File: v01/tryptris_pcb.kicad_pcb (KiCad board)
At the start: 2 copper layers, 133 parts, among them J1 USB_C_Receptacle_USB2.0, J2 I2C-L, J3 I2C-R, SW1 Reset, U1 ATmega32U4-AU, U2 MCP23017_SO, Y1 16Mhz

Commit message: PCB components roughly placed
* Removed duplicate resistors on D- and D+
* Roughly placed all components. MCU and IO expander and resistors are
  all on the back to save board space. I'm hoping that the board can fit
  inside the existing switch place outline.
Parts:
- removed R6, R7: 22, Resistor_SMD:R_0805_2012Metric
- C1, C2, C3, C4, C5, C6, C7, F2, J1, J2, J3, R10, R2, R3, R4, R5, R8, R9, U1, U2, Y1: moved to B.Cu
- moved R1 337.2 mm to (52.6, 34.3), turned to 270 degrees
- moved C5 318.2 mm to (92.6, 111.6), turned to 90 degrees
- moved C3 308.0 mm to (101.2, 97.3), turned to 90 degrees
- moved C6 306.3 mm to (103.4, 97.3), turned to 90 degrees
- moved U1 298.2 mm to (100.9, 108.1), turned to 270 degrees
- moved C2 289.5 mm to (112.5, 103.6), turned to 180 degrees
- moved C4 285.8 mm to (92.6, 105.1), turned to 270 degrees
- moved Y1 285.0 mm to (112.5, 107.1), turned to 90 degrees
- moved C1 275.8 mm to (112.5, 110.5)
- moved R8 221.3 mm to (95.8, 116.2)
- moved C7 201.5 mm to (106.0, 116.2)
- moved D45 145.2 mm to (314.6, 79.6)
- moved MX28 142.5 mm to (224.3, 45.1)
- moved D39 129.8 mm to (314.6, 60.7)
- moved R10 124.7 mm to (207.0, 118.0), turned to 180 degrees
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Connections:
- U1 pad 3: Net-(R7-Pad1) -> D-
- U1 pad 4: Net-(R6-Pad1) -> D+

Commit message: Made progress on the left side routing.
I am going to put the components on the bottom (except diodes), and
ports on the top so that the board can be lower to the table.

A bunch of routing for the left side is done after a few different
attempts.
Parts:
- J1: moved to F.Cu
- R1: moved to B.Cu
- moved R3 40.9 mm to (71.2, 30.9), turned to 270 degrees
- moved F2 31.2 mm to (73.7, 36.6)
- moved C2 31.1 mm to (83.0, 113.5), turned to 0 degrees
- moved C1 29.7 mm to (83.0, 106.6), turned to 180 degrees
- moved Y1 29.6 mm to (83.0, 110.0), turned to 270 degrees
- moved R2 29.0 mm to (83.2, 34.4), turned to 180 degrees
- moved R4 27.2 mm to (77.1, 47.4)
- moved C6 25.2 mm to (92.2, 119.8), turned to 270 degrees
- moved J1 25.1 mm to (77.6, 26.1), turned to 180 degrees
- moved C3 23.6 mm to (94.3, 119.8), turned to 270 degrees
- moved C7 22.2 mm to (90.6, 100.3), turned to 180 degrees
- moved R5 21.4 mm to (80.8, 47.4)
- moved R8 16.4 mm to (99.6, 100.3), turned to 180 degrees
- moved C4 14.0 mm to (104.4, 112.6), turned to 0 degrees
- moved C5 13.6 mm to (104.6, 105.2), turned to 0 degrees
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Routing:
- net GND: track 0.00 -> 202.3 mm, vias 0 -> 2
- net Row0-L: track 0.00 -> 197.0 mm, vias 0 -> 1
- net Row1-L: track 0.00 -> 169.9 mm, vias 0 -> 1
- net +5V: track 0.00 -> 159.4 mm, vias 0 -> 6
- net Row2-L: track 0.00 -> 149.6 mm, vias 0 -> 1
- net Col0: track 0.00 -> 127.7 mm
- net Row3-L: track 0.00 -> 126.2 mm, vias 0 -> 1
- net Col1: track 0.00 -> 124.4 mm
- net Net-(R1-Pad2): track 0.00 -> 110.9 mm
- net Col4: track 0.00 -> 97.6 mm
- net Col2: track 0.00 -> 96.6 mm, vias 0 -> 1
- net D-: track 0.00 -> 88.0 mm, vias 0 -> 2
- net D+: track 0.00 -> 83.8 mm, vias 0 -> 2
- net Col5: track 0.00 -> 60.0 mm
- net Col3: track 0.00 -> 57.0 mm
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- added copper zone on F.Cu, net (none)
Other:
- board outline added: 298.2 x 124.6 mm
- net class power added: clearance 0.2, trace_width 0.375, via_dia 0.8, via_drill 0.4

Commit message: Fiddle with wiring more.
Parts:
- J2: moved to F.Cu
- moved J2 19.8 mm to (142.9, 108.9), turned to 0 degrees
- renumbered F2 to F1
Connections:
- D25 pad 1: Row4L -> Row4-L
- D26 pad 1: Row4L -> Row4-L
- D27 pad 1: Row4L -> Row4-L
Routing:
- net Row4-L: track 0.00 -> 80.4 mm, vias 0 -> 1
- net Col3: track 57.0 -> 124.4 mm, vias 0 -> 1
- net Row4L: track 55.3 -> 0.00 mm
- net Col5: track 60.0 -> 105.3 mm
- net Col4: track 97.6 -> 126.3 mm, vias 0 -> 2
- net Net-(J1-PadB5): track 6.08 -> 8.14 mm, vias 0 -> 1
- net SCL-L: track 1.56 -> 0.00 mm
- net VCC: track 14.1 -> 14.4 mm, vias 2 -> 0
- added copper zone on B.Cu, net GND
- added copper zone on F.Cu, net GND
- removed copper zone on F.Cu, net (none)

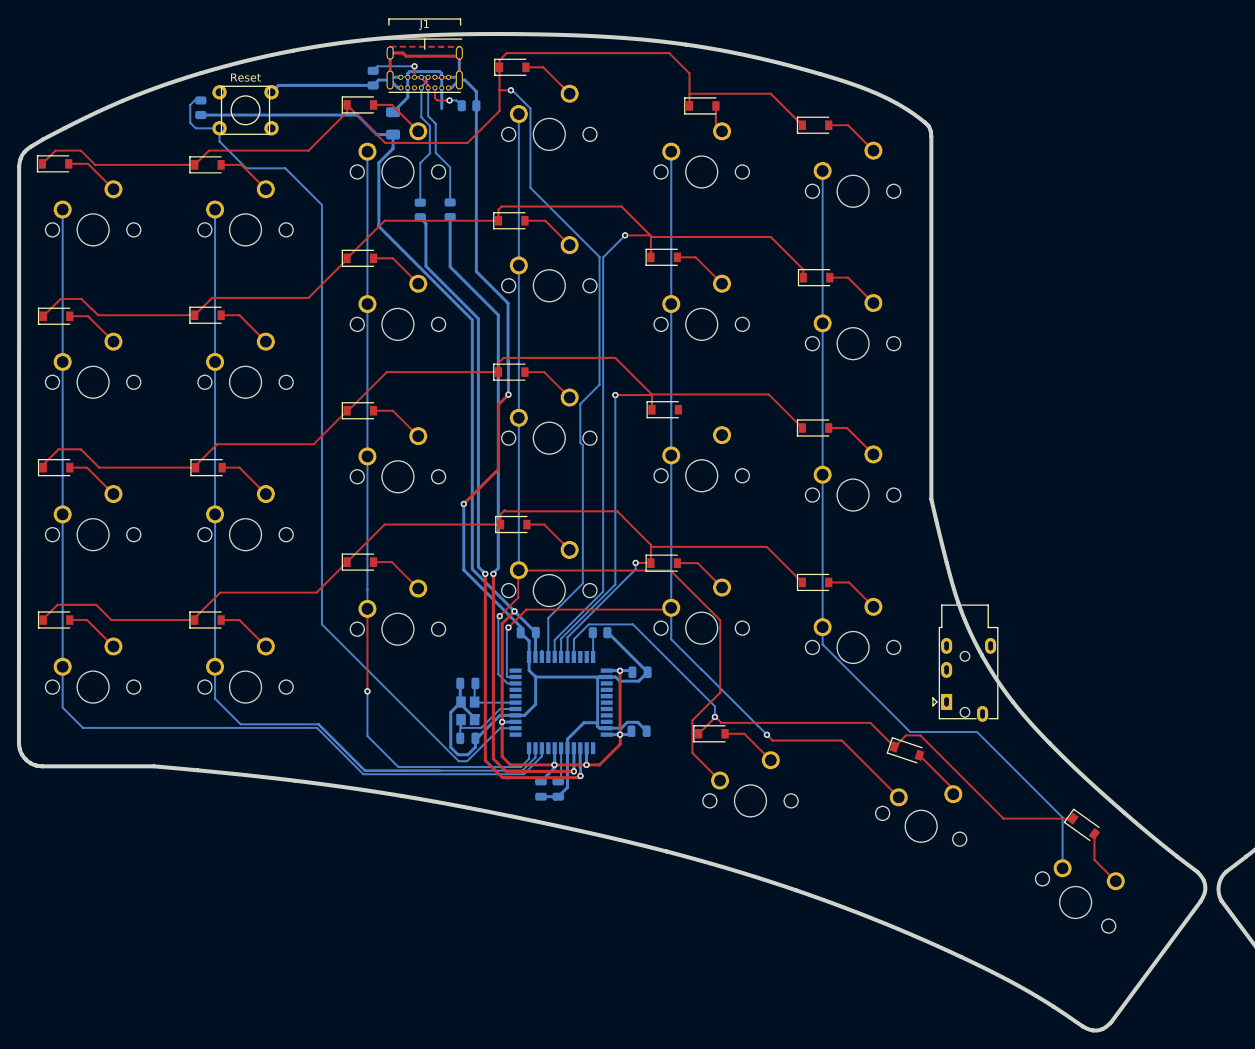
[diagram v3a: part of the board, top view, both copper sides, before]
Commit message: Move components to a block outside the switch matrix
* Having the ports top mounted will let the board be lower profile.
* Having the components on top looks kind of cool too.
* Roughly routed the entire left sideci!
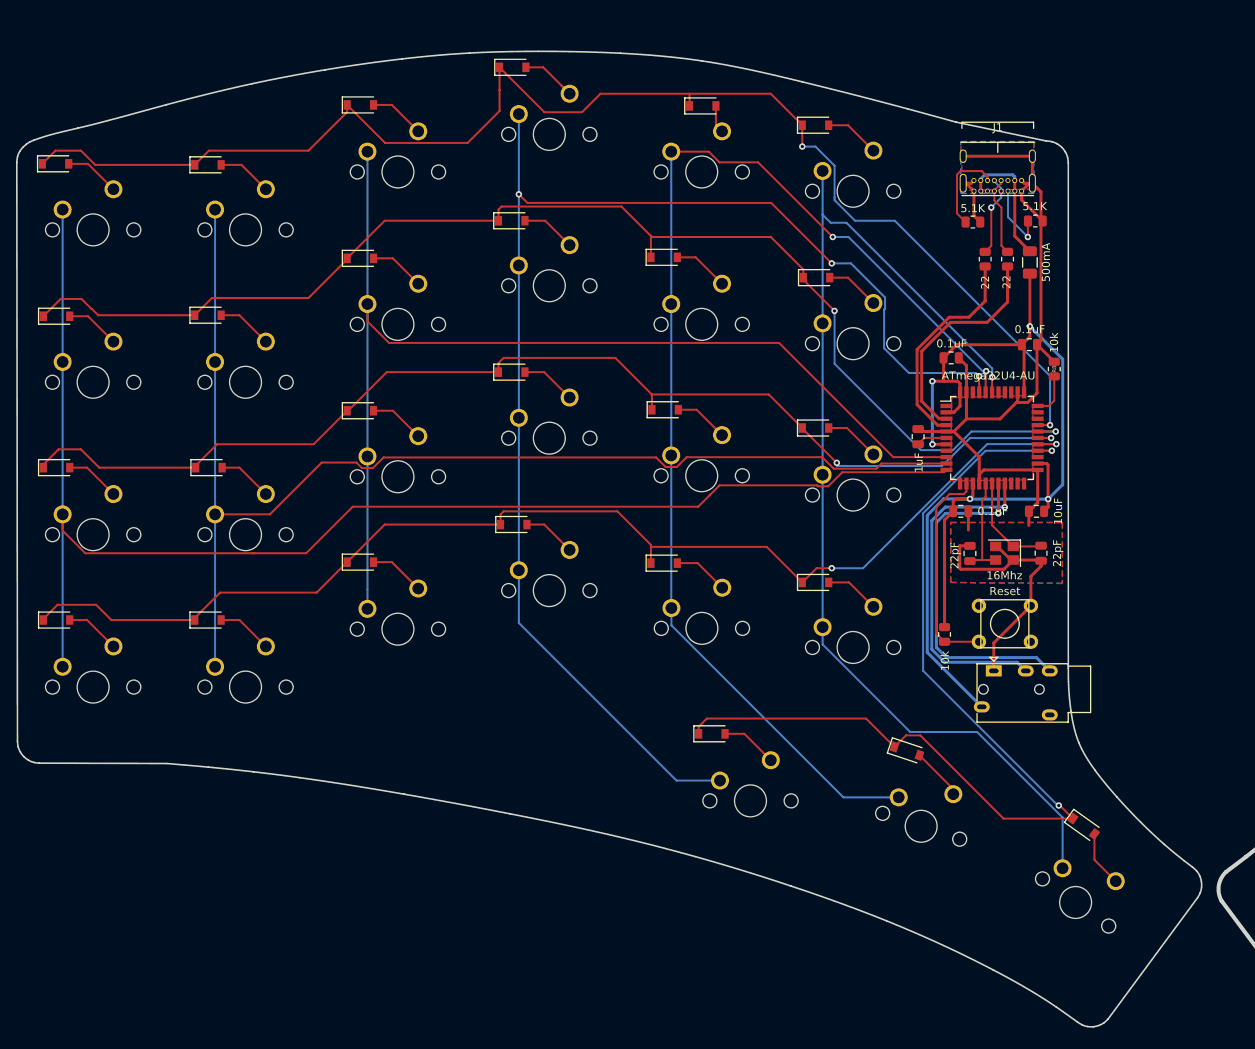
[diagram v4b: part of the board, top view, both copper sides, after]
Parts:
- C1, C2, C3, C4, C5, C6, C7, F1, R1, R2, R3, R4, R5, R8, U1, Y1: moved to F.Cu
- moved SW1 114.6 mm to (150.2, 99.2)
- moved R1 113.9 mm to (142.6, 100.5), turned to 270 degrees
- moved F1 81.5 mm to (153.3, 54.0)
- moved R3 77.1 mm to (146.2, 48.9), turned to 0 degrees
- moved C6 74.4 mm to (143.4, 65.9), turned to 0 degrees
- moved R4 73.7 mm to (150.5, 53.6)
- moved C1 73.5 mm to (154.7, 90.3), turned to 270 degrees
- moved J1 72.8 mm to (149.3, 39.0)
- moved R2 72.2 mm to (154.0, 48.8)
- moved Y1 69.9 mm to (150.1, 90.3), turned to 180 degrees
- moved C4 68.7 mm to (153.2, 64.3)
- moved R5 67.2 mm to (147.7, 53.6)
- moved C2 66.9 mm to (145.8, 90.4), turned to 90 degrees
- moved R8 65.6 mm to (156.3, 67.3), turned to 270 degrees
- moved C7 65.3 mm to (154.1, 85.1)
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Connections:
- U1 pad 11: Col2 -> Col0
- U1 pad 20: Col3 -> Net-(U1-Pad20)
- U1 pad 21: Col4 -> Net-(U1-Pad21)
- U1 pad 25: Col5 -> Net-(U1-Pad25)
- U1 pad 26: Row0-L -> Row4-L
- U1 pad 27: Row1-L -> Row3-L
- U1 pad 29: Row3-L -> Row1-L
- U1 pad 30: Row4-L -> Row0-L
- U1 pad 39: Net-(U1-Pad39) -> Col5
- U1 pad 40: Net-(U1-Pad40) -> Col4
- U1 pad 41: Net-(U1-Pad41) -> Col3
- U1 pad 9: Col0 -> Col2
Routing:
- net Net-(R1-Pad2): track 110.9 -> 27.7 mm
- net D-: track 88.0 -> 28.1 mm, vias 2 -> 0
- net GND: track 202.3 -> 144.2 mm, vias 2 -> 0
- net D+: track 83.8 -> 27.0 mm, vias 2 -> 0
- net Col0: track 127.7 -> 175.7 mm
- net Col3: track 124.4 -> 169.9 mm, vias 1 -> 3
- net SCL-L: track 0.00 -> 43.0 mm, vias 0 -> 1
- net Col2: track 96.6 -> 138.7 mm, vias 1 -> 0
- net SDA-L: track 0.00 -> 41.8 mm, vias 0 -> 1
- net Row4-L: track 80.4 -> 121.6 mm, vias 1 -> 2
- net Col5: track 105.3 -> 136.6 mm, vias 0 -> 1
- net Col1: track 124.4 -> 154.0 mm
- net Row0-L: track 197.0 -> 171.3 mm, vias 1 -> 2
- net Col4: track 126.3 -> 152.0 mm
- net Row3-L: track 126.2 -> 150.2 mm, vias 1 -> 2
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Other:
- board size 298.2 x 124.6 mm -> 298.5 x 124.5 mm

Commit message: Done first draft of right side wiring
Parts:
- J3, R10, R9, U2: moved to F.Cu
- moved U2 66.7 mm to (202.7, 75.6), turned to 0 degrees
- moved R10 17.6 mm to (201.8, 99.8), turned to 270 degrees
- moved R9 14.5 mm to (198.8, 99.9), turned to 270 degrees
- moved J3 12.8 mm to (203.5, 109.6), turned to 90 degrees
- moved J2 0.33 mm to (148.4, 105.0)
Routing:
- net Col11: track 0.00 -> 170.6 mm
- net Col10: track 0.00 -> 151.8 mm
- net Row3-R: track 0.00 -> 147.3 mm, vias 0 -> 2
- net Col8: track 0.00 -> 146.8 mm, vias 0 -> 1
- net Row0-R: track 0.00 -> 146.7 mm, vias 0 -> 2
- net Row1-R: track 0.00 -> 137.2 mm, vias 0 -> 2
- net Row2-R: track 0.00 -> 128.9 mm, vias 0 -> 2
- net Col9: track 0.00 -> 128.8 mm, vias 0 -> 1
- net Col7: track 0.00 -> 128.7 mm
- net Row4-R: track 0.00 -> 115.2 mm, vias 0 -> 2
- net Col6: track 0.00 -> 114.8 mm
- net VBUS: track 0.00 -> 82.7 mm, vias 0 -> 3
- net GND: track 144.2 -> 194.0 mm
- net SCL-R: track 0.00 -> 20.8 mm
- net SDA-R: track 0.00 -> 19.9 mm
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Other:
- board size 298.5 x 124.5 mm -> 298.8 x 122 mm

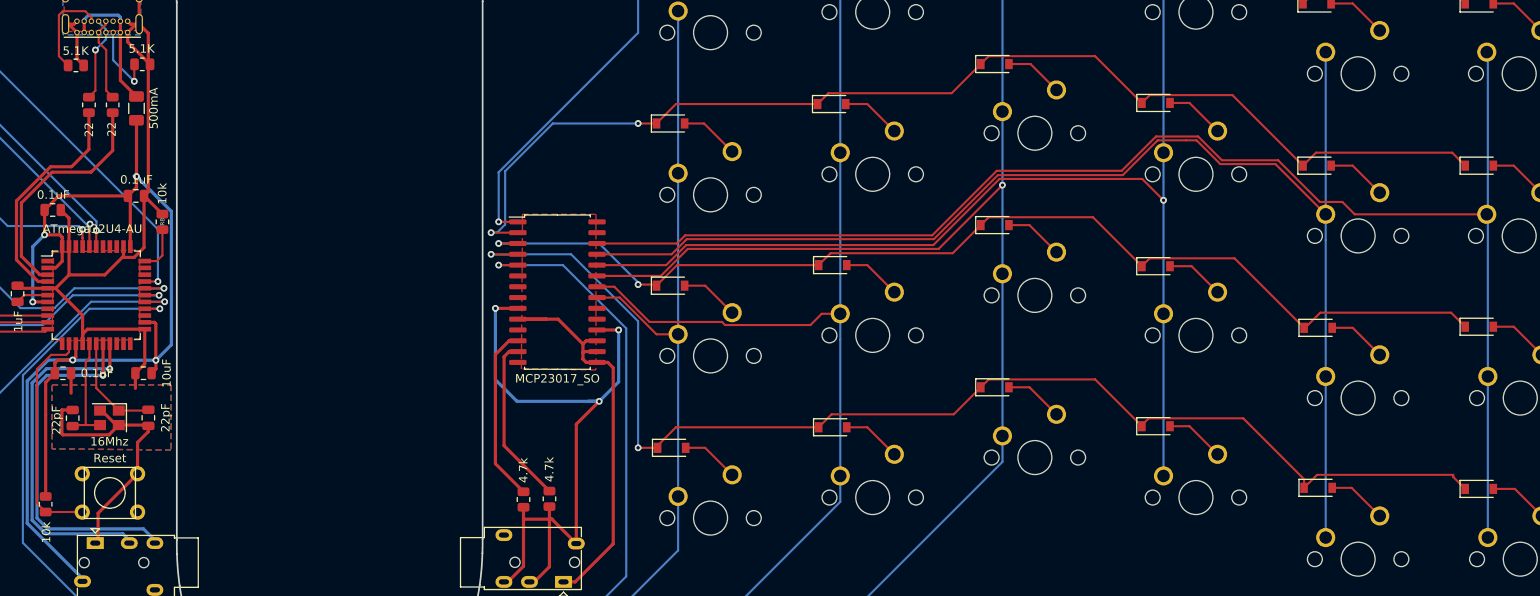
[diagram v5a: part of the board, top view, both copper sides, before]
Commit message: Fix missing connections and ground fill around crystal
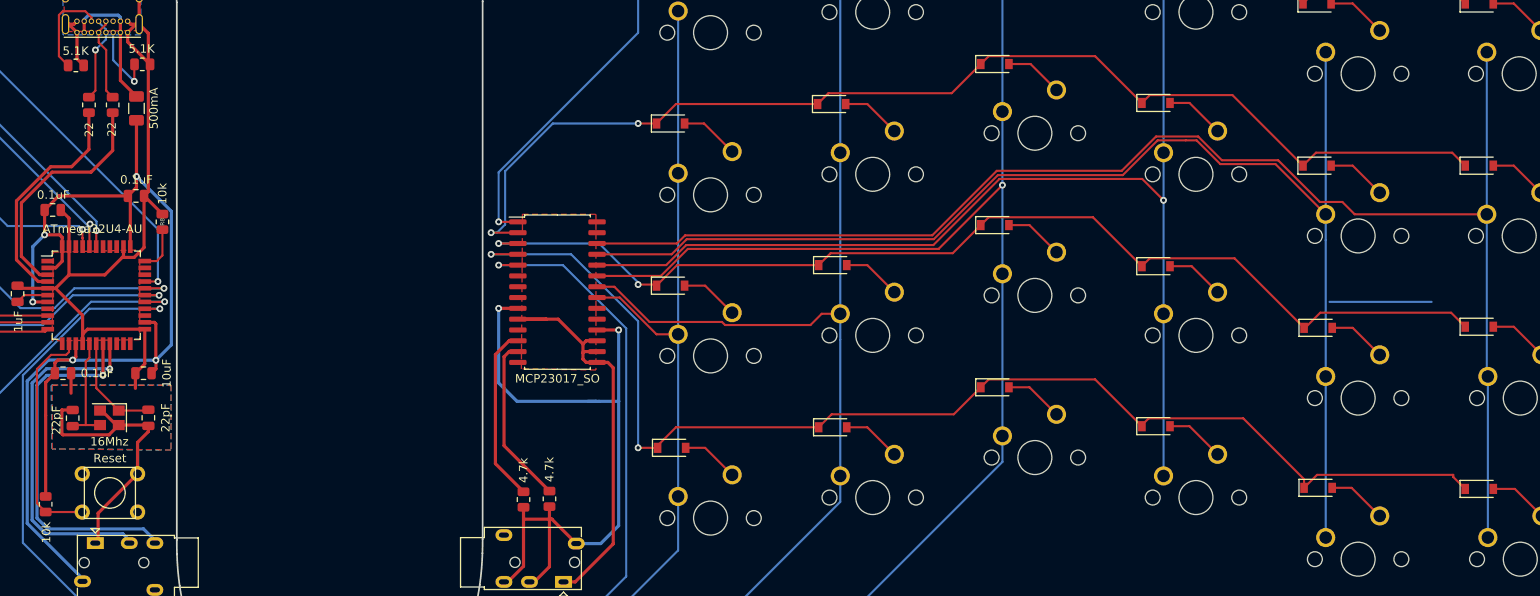
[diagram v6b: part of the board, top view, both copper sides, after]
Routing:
- net (no net): track 0.00 -> 12.0 mm
- net VBUS: track 82.7 -> 86.1 mm, vias 3 -> 2
- net GND: track 194.0 -> 196.9 mm
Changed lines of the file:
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@@
     (thickness 1.6)
     (drawings 358)
-    (tracks 798)
+    (tracks 803)
     (zones 0)
     (modules 131)
@@
   (gr_line (start 81.233 35.711) (end 81.233 49.711) (layer Dwgs.User) (width 0.2))
   (gr_line (start 86.233 68.961) (end 86.233 82.961) (layer Dwgs.User) (width 0.2))
+  (segment (start 305.435 76.708) (end 293.43901 76.708) (width 0.25) (layer B.Cu) (net 0))
   (segment (start 151.309 91.278) (end 151.209 91.178) (width 0.375) (layer F.Cu) (net 1))
   (segment (start 148.909 89.378) (end 149.009 89.478) (width 0.375) (layer F.Cu) (net 1))
@@
   (segment (start 201.422 78.74) (end 198.042 78.74) (width 0.375) (layer F.Cu) (net 1))
   (segment (start 202.819 78.74) (end 201.422 78.74) (width 0.375) (layer F.Cu) (net 1))
+  (segment (start 153.416 96.901) (end 153.416 93.98) (width 0.375) (layer B.Cu) (net 1))
   (segment (start 151.14 89.409) (end 151.209 89.478) (width 0.25) (layer F.Cu) (net 2))
   (segment (start 154.586 89.478) (end 154.686 89.378) (width 0.25) (layer F.Cu) (net 2))
@@
   (segment (start 198.755 107.761502) (end 198.755 102.235) (width 0.375) (layer F.Cu) (net 78))
   (segment (start 198.755 102.235) (end 198.755 100.838) (width 0.375) (layer F.Cu) (net 78))
-  (segment (start 204.954 105.101) (end 204.954 91.083) (width 0.375) (layer F.Cu) (net 78))
-  (via (at 207.645 88.392) (size 0.8) (drill 0.4) (layers F.Cu B.Cu) (net 78))
-  (segment (start 204.954 91.083) (end 207.645 88.392) (width 0.375) (layer F.Cu) (net 78))
-  (segment (start 207.645 88.392) (end 209.931 86.106) (width 0.375) (layer B.Cu) (net 78))
-  (via (at 209.931 80.01) (size 0.8) (drill 0.4) (layers F.Cu B.Cu) (net 78))
-  (segment (start 209.931 86.106) (end 209.931 80.01) (width 0.375) (layer B.Cu) (net 78))
   (segment (start 209.931 80.01) (end 207.391 80.01) (width 0.375) (layer F.Cu) (net 78))
-  (via (at 195.453 77.47) (size 0.8) (drill 0.4) (layers F.Cu B.Cu) (net 78))
-  (segment (start 195.453 77.47) (end 198.091 77.47) (width 0.375) (layer F.Cu) (net 78))
-  (segment (start 195.453 77.47) (end 195.453 85.852) (width 0.375) (layer B.Cu) (net 78))
   (segment (start 197.993 88.392) (end 207.264 88.392) (width 0.375) (layer B.Cu) (net 78))
-  (segment (start 195.453 85.852) (end 197.993 88.392) (width 0.375) (layer B.Cu) (net 78))
   (segment (start 207.264 88.392) (end 206.375 88.392) (width 0.375) (layer B.Cu) (net 78))
   (segment (start 207.645 88.392) (end 207.264 88.392) (width 0.375) (layer B.Cu) (net 78))
@@
   (segment (start 201.803 102.235) (end 201.803 100.758) (width 0.375) (layer F.Cu) (net 78))
   (segment (start 201.803 107.823) (end 201.803 102.235) (width 0.375) (layer F.Cu) (net 78))
+  (segment (start 198.091 77.47) (end 195.834 77.47) (width 0.375) (layer F.Cu) (net 78))
+  (via (at 195.834 77.47) (size 0.8) (drill 0.4) (layers F.Cu B.Cu) (net 78))
+  (segment (start 195.834 86.233) (end 197.993 88.392) (width 0.375) (layer B.Cu) (net 78))
+  (segment (start 195.834 77.47) (end 195.834 86.233) (width 0.375) (layer B.Cu) (net 78))
+  (segment (start 204.954 105.101) (end 207.827 105.101) (width 0.375) (layer B.Cu) (net 78))
+  (segment (start 207.827 105.101) (end 209.931 102.997) (width 0.375) (layer B.Cu) (net 78))
+  (via (at 209.931 80.01) (size 0.8) (drill 0.4) (layers F.Cu B.Cu) (net 78))
+  (segment (start 207.645 88.392) (end 209.931 88.392) (width 0.375) (layer B.Cu) (net 78))
+  (segment (start 209.931 88.392) (end 209.931 80.01) (width 0.375) (layer B.Cu) (net 78))
+  (segment (start 209.931 102.997) (end 209.931 88.392) (width 0.375) (layer B.Cu) (net 78))
   (segment (start 146.962 69.216) (end 146.939 69.193) (width 0.25) (layer F.Cu) (net 82))
   (segment (start 146.962 70.216) (end 146.962 69.216) (width 0.25) (layer F.Cu) (net 82))
@@
   (segment (start 292.989 66.421) (end 287.089999 60.521999) (width 0.25) (layer F.Cu) (net 89))
   (segment (start 273.242999 57.731999) (end 276.552999 57.731999) (width 0.25) (layer F.Cu) (net 89))
-  (segment (start 312.039 47.498) (end 312.039 104.394) (width 0.25) (layer B.Cu) (net 90))
   (segment (start 311.912 47.371) (end 312.039 47.498) (width 0.25) (layer B.Cu) (net 90))
   (segment (start 294.947001 64.970999) (end 296.397002 66.421) (width 0.25) (layer F.Cu) (net 90))
@@
   (segment (start 216.78436 69.85) (end 217.74237 68.89199) (width 0.25) (layer F.Cu) (net 90))
   (segment (start 207.391 69.85) (end 216.78436 69.85) (width 0.25) (layer F.Cu) (net 90))
+  (segment (start 311.912 47.371) (end 311.912 66.421) (width 0.25) (layer B.Cu) (net 90))
+  (segment (start 312.039 85.471) (end 312.039 104.394) (width 0.25) (layer B.Cu) (net 90))
+  (segment (start 311.912 85.344) (end 312.039 85.471) (width 0.25) (layer B.Cu) (net 90))
+  (segment (start 311.912 66.421) (end 311.912 85.344) (width 0.25) (layer B.Cu) (net 90))
   (segment (start 197.066 81.28) (end 195.453 82.893) (width 0.375) (layer F.Cu) (net 95))
   (segment (start 198.091 81.28) (end 197.066 81.28) (width 0.375) (layer F.Cu) (net 95))
@@
       )
     )
+  )
+  (zone (net 1) (net_name GND) (layer B.Cu) (hatch edge 0.508)
+    (connect_pads (clearance 0.508))
+    (min_thickness 0.254)
+    (fill yes (arc_segments 32) (thermal_gap 0.508) (thermal_bridge_width 0.508))
+    (polygon
+      (pts
+        (xy 157.353 94.107) (xy 143.383 93.98) (xy 143.256 86.487) (xy 157.353 86.487)
+      )
+    )
